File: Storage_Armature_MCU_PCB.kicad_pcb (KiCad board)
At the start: 4 copper layers, 163 x 221 mm, 366 parts, among them Q1 20N06, Q2 20N06, U10 NSI1200, U11 OPA333, U12 NSI1200, U13 OPA333, U14 USBLC6-2P6, U15 NSI1200, U16 OPA333, U17 NSI1200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

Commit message: VER1.0: добавил сухие контакты и логотип
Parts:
- added C111: 100n, Capacitor_SMD:C_0805_2012Metric_Pad1.18x1.45mm_HandSolder, F.Cu at (309.0, 207.0)
- added C112: 100n, Capacitor_SMD:C_0805_2012Metric_Pad1.18x1.45mm_HandSolder, F.Cu at (309.0, 204.5)
- added C113: 100n, Capacitor_SMD:C_0805_2012Metric_Pad1.18x1.45mm_HandSolder, F.Cu at (309.0, 202.0)
- added G***: LOGO, Logo_My:Logo_Company, F.Cu at (241.8, 109.2)
- added J2: ERROR, Connector_Molex:Molex_Mini-Fit_Jr_5569-06A2_2x03_P4.20mm_Horizontal, F.Cu at (301.9, 101.3)
- added R92: 3.3k, Resistor_SMD:R_1206_3216Metric_Pad1.30x1.75mm_HandSolder, F.Cu at (301.8, 112.5)
- added R93: 10k, Resistor_SMD:R_0805_2012Metric_Pad1.20x1.40mm_HandSolder, F.Cu at (311.2, 131.0)
- added R94: 3.3k, Resistor_SMD:R_1206_3216Metric_Pad1.30x1.75mm_HandSolder, F.Cu at (306.0, 112.5)
- added R95: 3.3k, Resistor_SMD:R_1206_3216Metric_Pad1.30x1.75mm_HandSolder, F.Cu at (310.2, 112.5)
- added R96: 10k, Resistor_SMD:R_0805_2012Metric_Pad1.20x1.40mm_HandSolder, F.Cu at (311.2, 128.8)
- added R97: 10k, Resistor_SMD:R_0805_2012Metric_Pad1.20x1.40mm_HandSolder, F.Cu at (311.2, 126.5)
- added U22: LTV-247, Package_SO:SOP-16_4.4x10.4mm_P1.27mm, F.Cu at (305.8, 120.8)
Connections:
- C105 pad 1: GND -> Net-(JP3-A)
- H2 pad 1: GND -> Net-(JP3-A)
- JP3 pad 1: GND -> Net-(JP3-A)
- R49 pad 1: GND -> Net-(JP3-A)
- U1 pad 21: unconnected-(U1-PA5-Pad21) -> /ERROR_LvL1
- U1 pad 22: unconnected-(U1-PA6-Pad22) -> /ERROR_LvL2
- U1 pad 23: unconnected-(U1-PA7-Pad23) -> /ERROR_LvL3
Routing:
- net /ERROR_LvL1: track 0.00 -> 104.0 mm, vias 0 -> 2
- net /ERROR_LvL2: track 0.00 -> 98.0 mm, vias 0 -> 2
- net /ERROR_LvL3: track 0.00 -> 97.3 mm, vias 0 -> 2
- net Net-(R92-Pad2): track 0.00 -> 6.47 mm
- net GND: track 123.6 -> 129.4 mm, vias 118 -> 124
- net Net-(R94-Pad2): track 0.00 -> 4.74 mm
- net /ERROR_LvL1_IN: track 0.00 -> 4.19 mm
- net /ERROR_LvL2_IN: track 0.00 -> 4.17 mm
- net /ERROR_LvL3_IN: track 0.00 -> 4.15 mm
- net Net-(R95-Pad2): track 0.00 -> 3.64 mm
- net GNDD: track 86.6 -> 89.7 mm, vias 89 -> 92
- net +3.3V: track 106.2 -> 109.2 mm, vias 63 -> 66
- added copper zone on B.Cu, net Net-(JP3-A)
- added copper zone on F.Cu, net Net-(JP3-A)
- added copper zone on In1.Cu, net Net-(JP3-A)
- added copper zone on In2.Cu, net Net-(JP3-A)
- removed copper zone on In2.Cu, net GND
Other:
- outline, holes or cut-outs redrawn
- board text added: "Control Board V1.0"
- board text added: "ERROR 123"

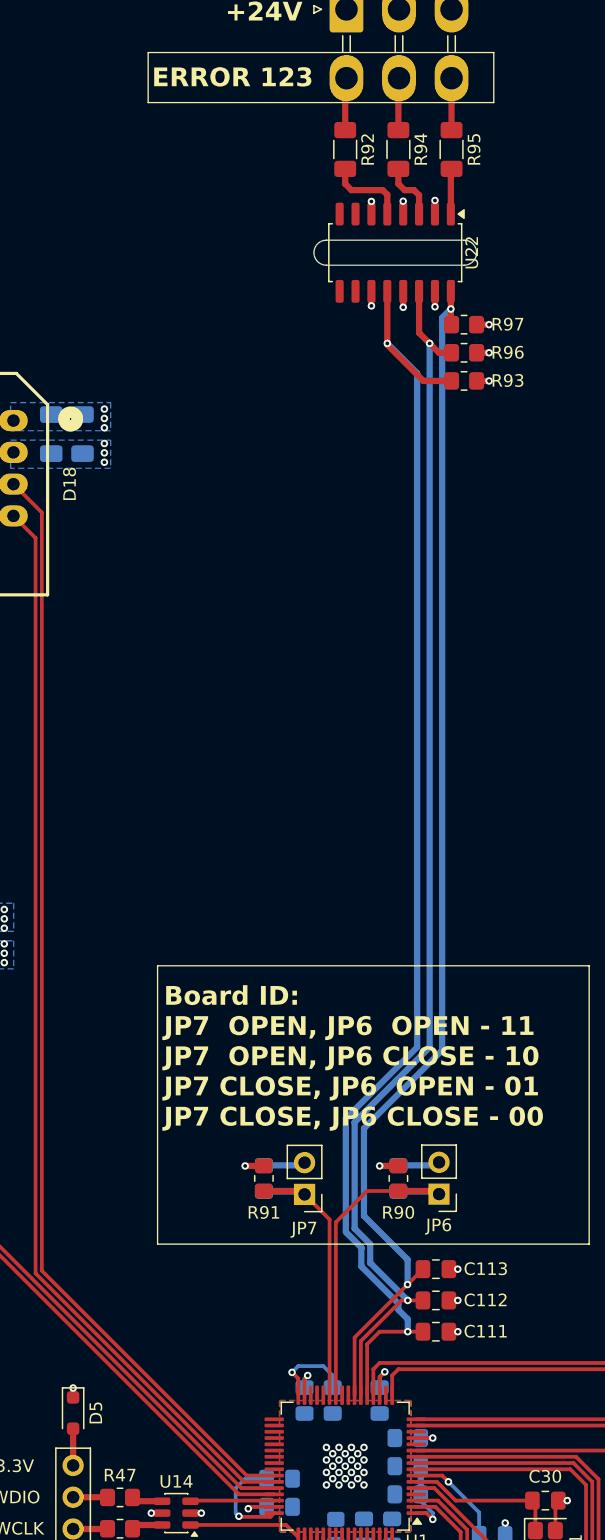
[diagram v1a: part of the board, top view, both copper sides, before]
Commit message: VER1.0: добавил светодиоды аварии и гребенку для анализатора
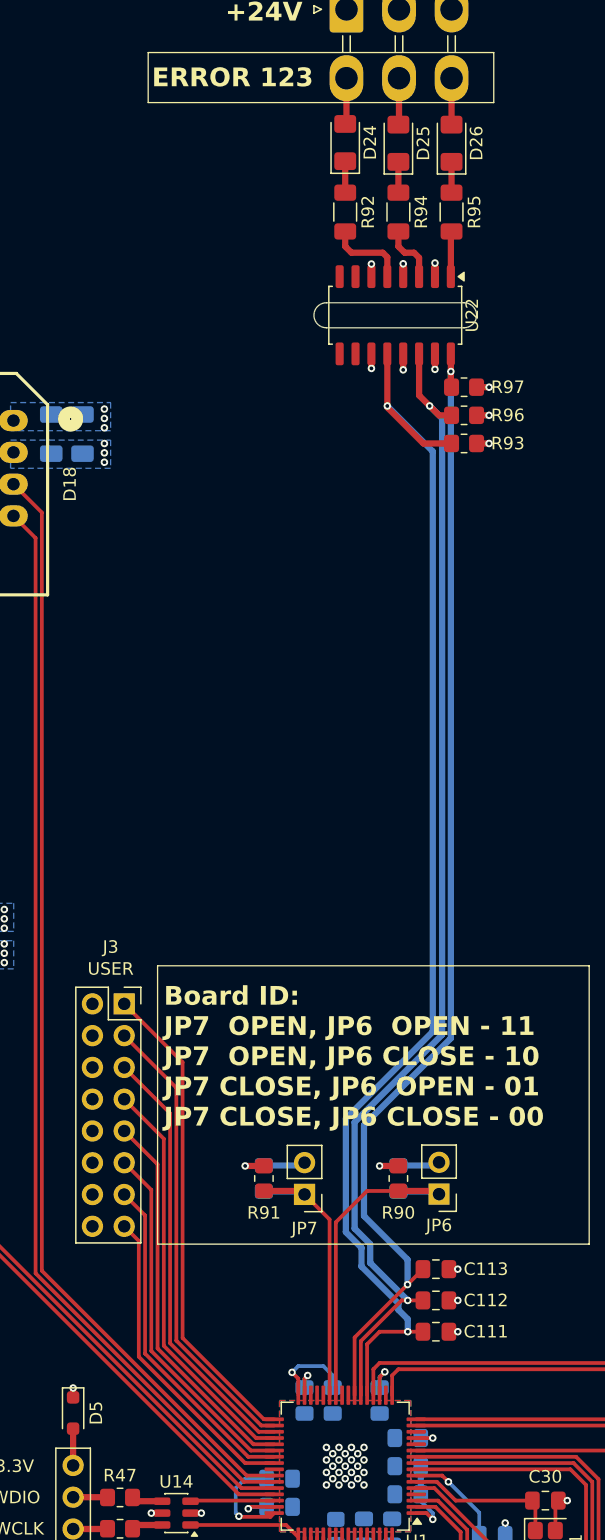
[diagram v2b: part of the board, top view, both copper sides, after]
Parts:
- added D24: ~, LED_SMD:LED_1206_3216Metric_Pad1.42x1.75mm_HandSolder, F.Cu at (301.8, 111.9)
- added D25: ~, LED_SMD:LED_1206_3216Metric_Pad1.42x1.75mm_HandSolder, F.Cu at (306.0, 112.0)
- added D26: ~, LED_SMD:LED_1206_3216Metric_Pad1.42x1.75mm_HandSolder, F.Cu at (310.2, 112.0)
- added J3: User, Connector_PinSocket_2.54mm:PinSocket_2x08_P2.54mm_Vertical, F.Cu at (284.1, 180.8)
- moved R92 5.00 mm to (301.8, 117.5)
- moved R93 5.00 mm to (311.2, 136.0)
- moved R94 5.00 mm to (306.0, 117.5)
- moved R95 5.00 mm to (310.2, 117.5)
- moved R96 5.00 mm to (311.2, 133.8)
- moved R97 5.00 mm to (311.2, 131.5)
- moved U22 5.00 mm to (305.8, 125.8)
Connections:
- R92 pad 1: /ERROR_LvL1_IN -> Net-(D24-K)
- R94 pad 1: /ERROR_LvL2_IN -> Net-(D25-K)
- R95 pad 1: /ERROR_LvL3_IN -> Net-(D26-K)
- U1 pad 33: unconnected-(U1-PB12-Pad33) -> /GPIO1
- U1 pad 34: unconnected-(U1-PB13-Pad34) -> /GPIO2
- U1 pad 35: unconnected-(U1-PB14-Pad35) -> /GPIO3
- U1 pad 36: unconnected-(U1-PB15-Pad36) -> /GPIO4
- U1 pad 37: unconnected-(U1-PC6-Pad37) -> /GPIO5
- U1 pad 38: unconnected-(U1-PC7-Pad38) -> /GPIO6
- U1 pad 39: unconnected-(U1-PC8-Pad39) -> /GPIO7
- U1 pad 40: unconnected-(U1-PC9-Pad40) -> /GPIO8
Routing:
- net /GPIO1: track 0.00 -> 38.7 mm
- net /GPIO2: track 0.00 -> 36.7 mm
- net /GPIO3: track 0.00 -> 34.8 mm
- net /GPIO4: track 0.00 -> 32.9 mm
- net /GPIO5: track 0.00 -> 31.0 mm
- net /GPIO6: track 0.00 -> 29.1 mm
- net /GPIO7: track 0.00 -> 27.1 mm
- net /GPIO8: track 0.00 -> 25.3 mm
- net /ERROR_LvL3: track 97.3 -> 92.3 mm
- net /ERROR_LvL2: track 98.0 -> 93.8 mm
- net /ERROR_LvL1: track 104.0 -> 100.0 mm
- net Net-(D24-K): track 0.00 -> 2.52 mm
- net Net-(D26-K): track 0.00 -> 2.46 mm
- net Net-(D25-K): track 0.00 -> 2.46 mm
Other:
- outline, holes or cut-outs redrawn
- board text added: "USER"
